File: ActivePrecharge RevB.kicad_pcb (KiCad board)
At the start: 2 copper layers, 59 parts, among them IC1 AMC1350DWVR, IC2 AMC1350DWVR, U1 LT1963AEST-3.3_TRPBF, U2 TLV9001IDBVR, U3 TLV9001IDBVR

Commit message: First Initial PCB Layout Finished
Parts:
- removed D5, D6: LED, LED_SMD:LED_0603_1608Metric_Pad1.05x0.95mm_HandSolder
- removed HV_Connector1: Conn_01x03, Connector_Molex:Molex_Nano-Fit_105309-xx03_1x03_P2.50mm_Vertical
- removed Motor_Contactor_Connector1, Precharge_Contactor_Connector1: Conn_01x04, Connector_Molex:Molex_Nano-Fit_105309-xx04_1x04_P2.50mm_Vertical
- removed R12, R14: 10k, Resistor_SMD:R_0603_1608Metric_Pad0.98x0.95mm_HandSolder
- removed R13: 15k, Resistor_SMD:R_0603_1608Metric_Pad0.98x0.95mm_HandSolder
- removed R15, R16: 10, Resistor_SMD:R_0603_1608Metric_Pad0.98x0.95mm_HandSolder
- removed VCU_Connector1: Conn_02x06_Counter_Clockwise, Connector_Molex:Molex_Nano-Fit_105310-xx12_2x06_P2.50mm_Vertical
- added C17: 100nF, Capacitor_SMD:C_0603_1608Metric_Pad1.08x0.95mm_HandSolder, F.Cu at (162.7, 100.3)
- added C20: 0.1uF, Capacitor_SMD:C_0603_1608Metric_Pad1.08x0.95mm_HandSolder, F.Cu at (157.5, 108.9)
- added C21: 0.47uF, Capacitor_SMD:C_0603_1608Metric_Pad1.08x0.95mm_HandSolder, F.Cu at (159.1, 111.4)
- added C22: 10nF, Capacitor_SMD:C_0603_1608Metric_Pad1.08x0.95mm_HandSolder, F.Cu at (180.2, 95.1)
- added C23: 10nF, Capacitor_SMD:C_0603_1608Metric_Pad1.08x0.95mm_HandSolder, F.Cu at (179.7, 105.4)
- added F3: 15A, ActivePrecharge-RevB:FUSE_3568, F.Cu at (170.2, 80.5)
- added H1: MountingHole_Pad, MountingHole:MountingHole_3.2mm_M3_Pad_TopBottom, F.Cu at (104.0, 63.6)
- added H2: MountingHole_Pad, MountingHole:MountingHole_3.2mm_M3_Pad_TopBottom, F.Cu at (192.8, 63.6)
- added H3: MountingHole_Pad, MountingHole:MountingHole_3.2mm_M3_Pad_TopBottom, F.Cu at (103.7, 116.3)
- added H4: MountingHole_Pad, MountingHole:MountingHole_3.2mm_M3_Pad_TopBottom, F.Cu at (193.0, 116.3)
- added IC3: ZXRE160AET5TA, ActivePrecharge-RevB:SOT95P280X100-5N, F.Cu at (161.6, 108.7)
- added J1: HVConnector, Connector_Molex:Molex_Nano-Fit_105309-xx03_1x03_P2.50mm_Vertical, F.Cu at (109.9, 71.8)
- added J2: ExportConnector, Connector_Molex:Molex_Nano-Fit_105310-xx12_2x06_P2.50mm_Vertical, F.Cu at (187.8, 84.2)
- added J3: PrechargeContactor, Connector_Molex:Molex_Nano-Fit_105309-xx04_1x04_P2.50mm_Vertical, F.Cu at (183.2, 70.0)
- added J4: MainContactor, Connector_Molex:Molex_Nano-Fit_105309-xx04_1x04_P2.50mm_Vertical, F.Cu at (190.8, 108.7)
- added R18: 1k, Resistor_SMD:R_0603_1608Metric_Pad0.98x0.95mm_HandSolder, F.Cu at (161.6, 106.1)
- added R19: 5.1k, Resistor_SMD:R_0603_1608Metric_Pad0.98x0.95mm_HandSolder, F.Cu at (162.9, 113.1)
- added R20: 15k, Resistor_SMD:R_0603_1608Metric_Pad0.98x0.95mm_HandSolder, F.Cu at (159.1, 113.1)
- added R21: 2.49k, Resistor_SMD:R_0603_1608Metric_Pad0.98x0.95mm_HandSolder, F.Cu at (170.9, 94.0)
- added R22: 15k, Resistor_SMD:R_0603_1608Metric_Pad0.98x0.95mm_HandSolder, F.Cu at (170.9, 95.9)
- added R23: 2.49k, Resistor_SMD:R_0603_1608Metric_Pad0.98x0.95mm_HandSolder, F.Cu at (175.5, 86.6)
- added R24: 15k, Resistor_SMD:R_0603_1608Metric_Pad0.98x0.95mm_HandSolder, F.Cu at (175.5, 90.8)
- added R25: 10, Resistor_SMD:R_0603_1608Metric_Pad0.98x0.95mm_HandSolder, F.Cu at (180.2, 93.1)
- added R26: 2.49k, Resistor_SMD:R_0603_1608Metric_Pad0.98x0.95mm_HandSolder, F.Cu at (170.9, 106.1)
- added R27: 2.49k, Resistor_SMD:R_0603_1608Metric_Pad0.98x0.95mm_HandSolder, F.Cu at (170.9, 99.0)
- added R28: 15k, Resistor_SMD:R_0603_1608Metric_Pad0.98x0.95mm_HandSolder, F.Cu at (170.9, 102.0)
- added R29: 15k, Resistor_SMD:R_0603_1608Metric_Pad0.98x0.95mm_HandSolder, F.Cu at (170.9, 107.7)
- added R30: 10, Resistor_SMD:R_0603_1608Metric_Pad0.98x0.95mm_HandSolder, F.Cu at (179.7, 103.5)
- added TP10: 3V3, TestPoint:TestPoint_Pad_1.0x1.0mm, F.Cu at (168.4, 70.8)
- added TP11: LVGND, TestPoint:TestPoint_Pad_1.0x1.0mm, F.Cu at (173.9, 112.2)
- C1, C2: footprint ActivePrecharge-RevB:CAPC1709X100N -> Capacitor_SMD:C_0805_2012Metric_Pad1.18x1.45mm_HandSolder
- C10, C11: value 1uF -> 1nF
- C13, C14, C6: value 100nF -> 1uF
- C15: value 10nF -> 1uF
- C16: value 10nF -> 100nF
- C3, C4: footprint Capacitor_SMD:C_0603_1608Metric_Pad1.08x0.95mm_HandSolder -> ActivePrecharge-RevB:CAPC1709X100N
- C5: value 100nF -> 1uF; footprint Capacitor_SMD:C_0603_1608Metric_Pad1.08x0.95mm_HandSolder -> ActivePrecharge-RevB:CAPC1709X100N
- C7: value 1nF -> 1uF
- C8: value 1nF -> 100nF
- C9: value 1uF -> 100nF
- D2, D3: value RSX068MP2STR -> LED; footprint ActivePrecharge-RevB:RSX068MP2STR -> LED_SMD:LED_0603_1608Metric_Pad1.05x0.95mm_HandSolder
- F1, F2: value Fuse -> 15A
- R10, R8: value 2.49k -> 100k
- R11: value 15k -> 2.49k
- R4: value 120 -> 330; footprint Resistor_SMD:R_0603_1608Metric_Pad0.98x0.95mm_HandSolder -> ActivePrecharge-RevB:RES_PWR263S-35-3300F
- R5: value 768 -> 1k
- R6: value 120 -> 1k
- R7: value 100k -> 1k
- R9: value 100k -> 2.49k
- U1: value LT1963AEST-3.3_TRPBF -> LT1963AEST-3.3#TRPBF
- moved TP1 72.9 mm to (116.0, 112.2)
- moved TP2 71.4 mm to (110.0, 112.2)
- moved TP7 69.8 mm to (147.8, 113.0), turned to 180 degrees
- moved R4 69.3 mm to (127.3, 109.6)
- moved TP3 63.5 mm to (116.0, 108.8)
- moved TP9 63.2 mm to (170.2, 112.2)
- moved R11 63.0 mm to (138.4, 101.6), turned to 90 degrees
- moved C15 61.6 mm to (165.7, 100.3), turned to -90 degrees
- moved C9 57.3 mm to (141.5, 97.8), turned to 90 degrees
- moved C11 55.8 mm to (146.0, 101.5), turned to -90 degrees
- moved C7 50.8 mm to (141.5, 101.5), turned to -90 degrees
- moved C16 50.6 mm to (166.7, 91.0), turned to -90 degrees
- moved C10 49.2 mm to (146.0, 92.4), turned to -90 degrees
- moved U3 47.1 mm to (175.3, 104.5)
- moved C13 47.0 mm to (146.0, 97.7), turned to 90 degrees
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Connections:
- C10 pad 1: REG_3V3 -> /Voltage_Sense/Vin1
- C11 pad 1: 3V3 -> /Voltage_Sense/Vin2
- C11 pad 2: LVGND -> HVGND
- C12 pad 1: 3V3 -> REG_3V3
- C12 pad 2: LVGND -> HVGND
- C13 pad 1: 3V3 -> REG_3V3
- C13 pad 2: LVGND -> HVGND
- C15 pad 1: /VOut1 -> 3V3
- C16 pad 1: /VOut2 -> 3V3
- C3 pad 1: /Voltage_Sense/Vin1 -> 3V3
- C3 pad 2: HVGND -> LVGND
- C4 pad 1: /Voltage_Sense/Vin2 -> HVGND
- C4 pad 2: HVGND -> ISO_5V
- C5 pad 1: REG_3V3 -> 3V3
- C5 pad 2: HVGND -> LVGND
- C6 pad 1: REG_3V3 -> /Voltage_Sense/Vin1
- C7 pad 1: /Voltage_Sense/Vin1 -> /Voltage_Sense/Vin2
- C8 pad 1: /Voltage_Sense/Vin2 -> REG_3V3
- D2 pad 1: Net-(D2-K) -> HVGND
- D2 pad 2: HVGND -> Net-(D2-A)
- D3 pad 1: HV- -> HVGND
- F2 pad 2: Net-(D3-A) -> HV-
- R10 pad 1: HVGND -> /Voltage_Sense/Vin2
- R10 pad 2: /Voltage_Sense/Vin2 -> HV-
- R11 pad 1: Net-(U2-OUT) -> HVGND
- R11 pad 2: Net-(U2-IN-) -> /Voltage_Sense/Vin2
- R4 pad 1: REG_3V3 -> HV-
- R4 pad 2: Net-(D4-A) -> HV+
- R5 pad 1: ISO_5V -> REG_3V3
- R5 pad 2: Net-(D5-A) -> Net-(D2-A)
- R6 pad 1: 3V3 -> ISO_5V
- R6 pad 2: Net-(D6-A) -> Net-(D3-A)
- R7 pad 1: /Voltage_Sense/Vin1 -> 3V3
- R7 pad 2: HV+ -> Net-(D4-A)
- R8 pad 1: HVGND -> /Voltage_Sense/Vin1
- R8 pad 2: /Voltage_Sense/Vin1 -> HV+
- R9 pad 1: /Voltage_Sense/Vin2 -> HVGND
- R9 pad 2: HV- -> /Voltage_Sense/Vin1
- U1 pad 4: HVGND -> (no net)
- U2 pad 1: Net-(U2-OUT) -> Net-(U2-+)
- U2 pad 2: LVGND -> Net-(U2--)
- U2 pad 3: /Voltage_Sense/V1 -> 3V3
- U2 pad 4: Net-(U2-IN-) -> LVGND
- U2 pad 5: 3V3 -> Net-(R22-Pad1)
- U3 pad 2: LVGND -> Net-(U3--)
- U3 pad 3: /Voltage_Sense/V2 -> 3V3
- U3 pad 4: Net-(U3-IN-) -> LVGND
- U3 pad 5: 3V3 -> Net-(R29-Pad1)
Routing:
- net 3V3: track 0.00 -> 77.1 mm, vias 0 -> 4
- net HV+: track 0.00 -> 38.9 mm, vias 0 -> 2
- net /Voltage_Sense/Vin1: track 0.00 -> 37.6 mm
- net REG_3V3: track 0.00 -> 36.6 mm, vias 0 -> 3
- net /Voltage_Sense/V1: track 0.00 -> 36.3 mm
- net REG_0V8: track 0.00 -> 32.6 mm, vias 0 -> 2
- net /Pre-: track 0.00 -> 31.1 mm
- net HV-: track 0.00 -> 28.1 mm, vias 0 -> 3
- net /VOut2: track 0.00 -> 27.5 mm
- net /Voltage_Sense/Vin2: track 0.00 -> 25.6 mm
- net /Motor-: track 0.00 -> 25.5 mm
- net /MotorSense-: track 0.00 -> 25.0 mm
- net /PreSense-: track 0.00 -> 23.5 mm
- net /Voltage_Sense/V2: track 0.00 -> 22.9 mm, vias 0 -> 2
- net /PreSense+: track 0.00 -> 22.0 mm
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- added copper zone on B.Cu, net 3V3
- added copper zone on F.Cu, net HV+
- added copper zone on F.Cu, net HV-
- added copper zone on F.Cu, net HVGND
- added copper zone on F.Cu, net LVGND
- added copper zone on B.Cu, net REG_3V3
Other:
- board outline added: 98 x 61 mm

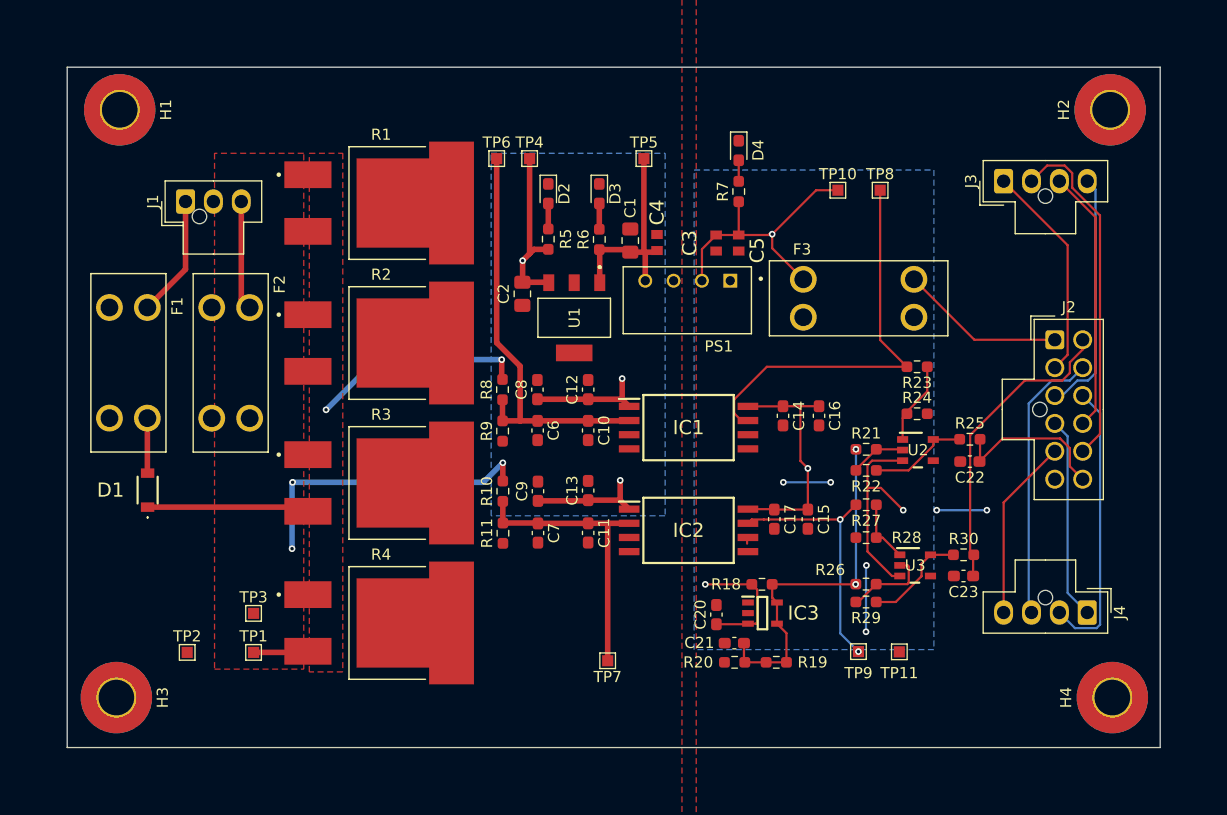
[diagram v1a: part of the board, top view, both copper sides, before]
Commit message: All layout changes made except new symbol for precharge resistors for heat dissipation and new fuses
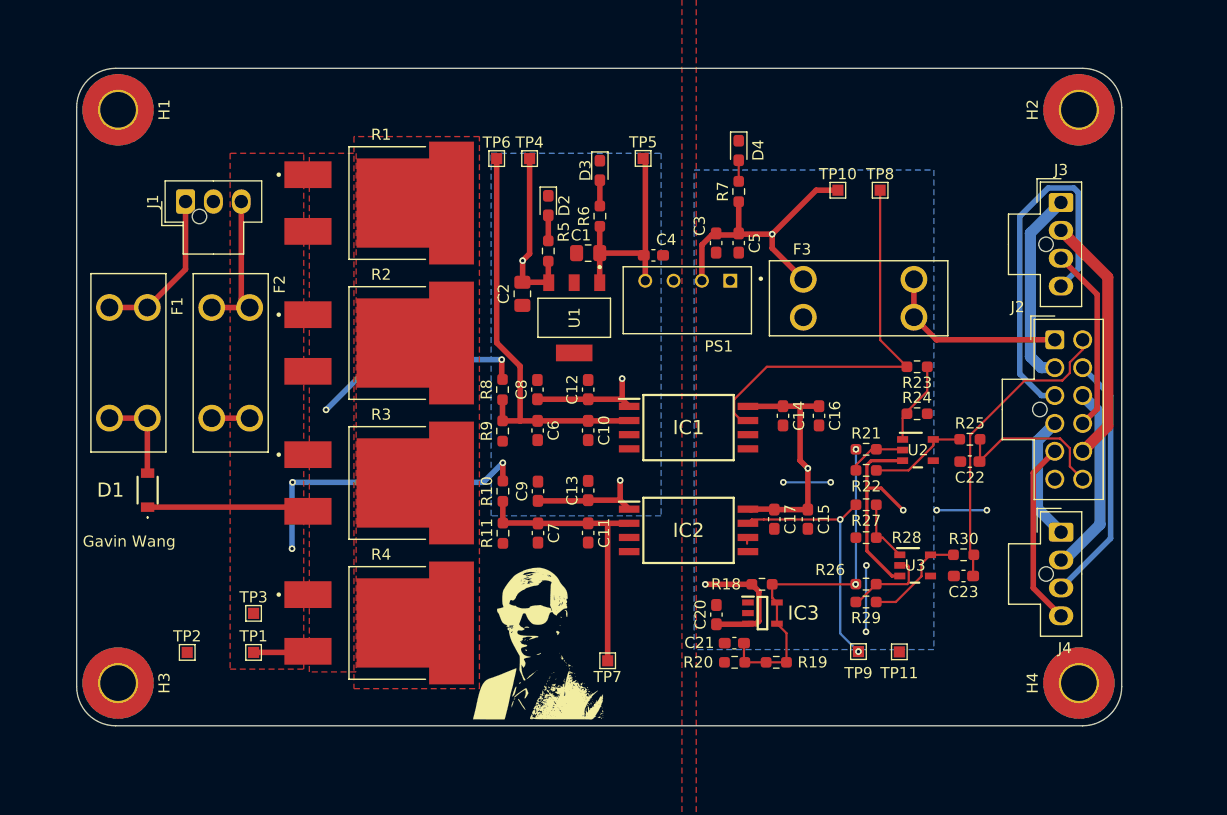
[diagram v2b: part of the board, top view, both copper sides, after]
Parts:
- added LOGO1: Dr. Hallock, UTSVT-Logos:Hallock_Image_Tiny, F.Cu at (141.0, 111.3)
- added LOGO2: Dr. Hallock, UTSVT-Logos:LHRs_LOGO, F.Cu at (117.5, 63.2)
- C3, C4, C5: footprint ActivePrecharge-RevB:CAPC1709X100N -> Capacitor_SMD:C_0603_1608Metric_Pad1.08x0.95mm_HandSolder
- F1, F2, F3: value 15A -> 1.5A
- moved J4 7.58 mm to (188.4, 101.5), turned to 0 degrees
- moved J3 5.49 mm to (188.4, 71.9), turned to 0 degrees
- moved C1 3.94 mm to (146.0, 76.5), turned to 180 degrees
- moved H4 3.27 mm to (190.0, 115.0)
- moved H2 2.80 mm to (190.0, 63.6)
- moved D3 2.09 mm to (147.1, 69.0)
- moved R6 2.09 mm to (147.1, 73.1)
- moved H3 1.31 mm to (103.8, 115.0)
- moved C4 1.20 mm to (151.8, 76.7), turned to 180 degrees
- moved D2 1.06 mm to (142.4, 72.2)
- moved R5 1.06 mm to (142.4, 76.3)
- moved H1 0.15 mm to (103.8, 63.6)
- moved TP5 0.07 mm to (150.9, 68.0)
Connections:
- U1 pad 4: (no net) -> HVGND
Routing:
- net /PreSense+: track 22.0 -> 33.6 mm
- net /Pre-: track 31.1 -> 22.5 mm
- net /Motor-: track 25.5 -> 17.0 mm
- net /Motor+: track 18.2 -> 11.3 mm
- net /PreSense-: track 23.5 -> 16.7 mm
- net Net-(D1-A): track 4.94 -> 8.34 mm
- net Net-(J1-Pin_3): track 9.82 -> 13.2 mm
- net Net-(J1-Pin_1): track 10.9 -> 14.3 mm
- net HV-: track 28.1 -> 31.5 mm
- net /MotorSense-: track 25.0 -> 22.6 mm
- net /Pre+: track 19.6 -> 17.6 mm
- net Net-(J2-Pin_1): track 14.9 -> 16.9 mm
- net 3V3: track 77.1 -> 78.7 mm
- net ISO_5V: track 19.3 -> 20.3 mm
- added copper zone on F.Cu, net (none)
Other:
- board size 98 x 61 mm -> 93.7 x 58.9 mm
- board text added: "Gavin Wang"

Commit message: All new comments addressed
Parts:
- moved V1 3.81 mm to (172.2, 67.0)
- moved 3V3 3.81 mm to (168.4, 67.0)
- moved LOGO2 2.64 mm to (115.3, 64.8)
- moved REG_3V3 2.50 mm to (143.1, 67.0)
- moved ExportConnector 1.16 mm to (187.8, 83.1)
- moved PrechargeContactor 1.16 mm to (188.3, 70.8)
- moved MainContactor 1.16 mm to (188.4, 100.3)
- moved Vin1 0.97 mm to (137.8, 67.0)
- moved ISO_5V 0.96 mm to (151.0, 67.0)
- moved C22 0.53 mm to (179.7, 95.1)
- moved R25 0.53 mm to (179.7, 93.1)
- moved Vin2 0.50 mm to (147.8, 112.5)
- moved V2 0.42 mm to (170.5, 112.5)
- moved LVGND 0.30 mm to (173.9, 112.5)
- renumbered TP10 to 3V3, J2 to ExportConnector, TP1 to HV+, TP3 to HV-, J1 to HVConnector, TP2 to HV_GND, TP5 to ISO_5V, TP11 to LVGND, J4 to MainContactor, J3 to PrechargeContactor, TP4 to REG_3V3, TP8 to V1, TP9 to V2, TP6 to Vin1, TP7 to Vin2
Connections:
- R1 pad 3: (no net) -> /HEAT_DISSIPATION
- R2 pad 3: (no net) -> /HEAT_DISSIPATION
- R3 pad 3: (no net) -> /HEAT_DISSIPATION
- R4 pad 3: (no net) -> /HEAT_DISSIPATION
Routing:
- net LVGND: track 15.3 -> 4.84 mm
- net HV-: track 31.5 -> 25.6 mm, vias 3 -> 7
- net REG_3V3: track 36.6 -> 32.4 mm, vias 3 -> 5
- net /Voltage_Sense/V1: track 36.3 -> 40.1 mm
- net 3V3: track 78.7 -> 75.5 mm, vias 4 -> 3
- net /VOut2: track 27.5 -> 29.1 mm
- net /Voltage_Sense/V2: track 22.9 -> 24.2 mm
- net /Voltage_Sense/Vin1: track 37.6 -> 38.6 mm
- net ISO_5V: track 20.3 -> 21.2 mm
- net REG_0V8: track 32.6 -> 33.4 mm
- net Net-(J2-Pin_1): track 16.9 -> 16.3 mm
- net Net-(R22-Pad1): track 8.95 -> 8.43 mm
- net /Voltage_Sense/Vin2: track 25.6 -> 25.1 mm
- net HVGND: vias 0 -> 1
- net /HEAT_DISSIPATION: vias 0 -> 24
- added copper zone on B.Cu, net /HEAT_DISSIPATION
- added copper zone on F.Cu, net /HEAT_DISSIPATION
- added copper zone on B.Cu, net HV-
- added copper zone on B.Cu, net HVGND
- added copper zone on B.Cu, net LVGND
- added copper zone on F.Cu, net REG_3V3
- removed copper zone on F.Cu, net (none)
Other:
- board text added: "1.5A"

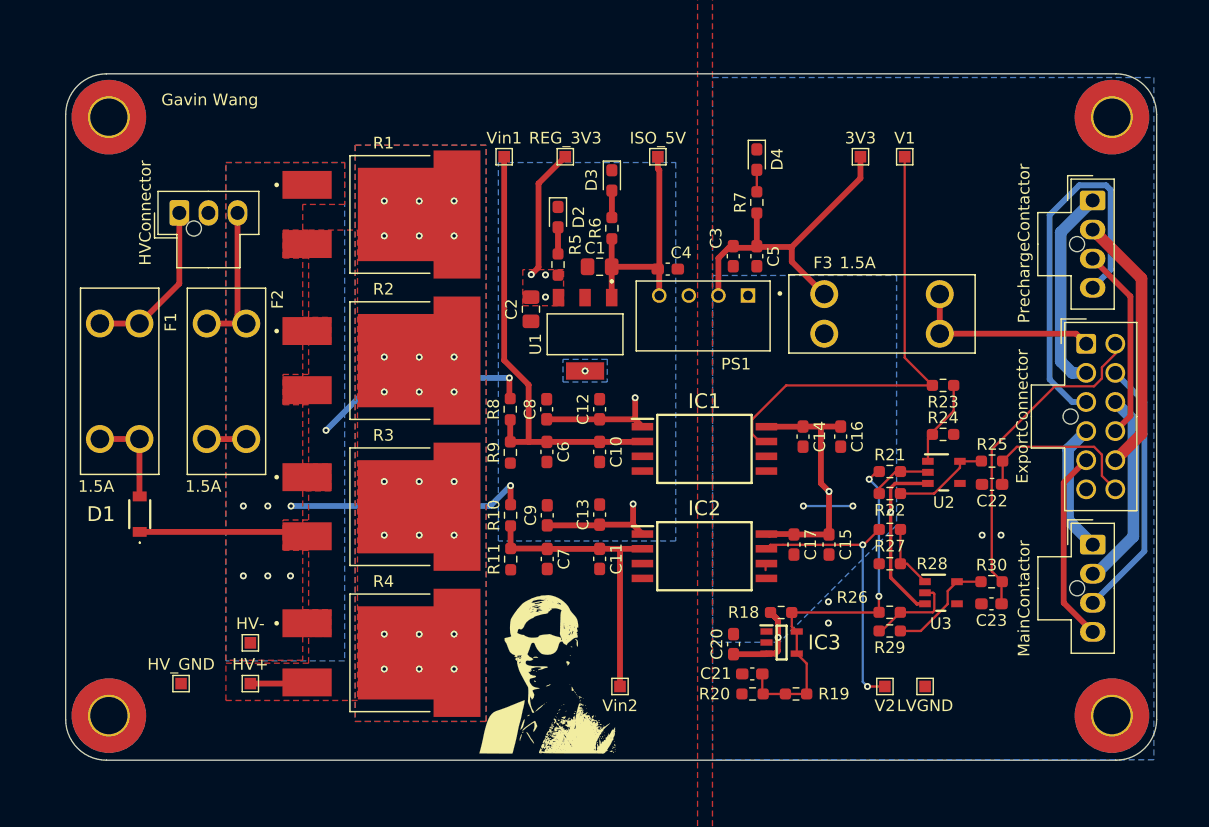
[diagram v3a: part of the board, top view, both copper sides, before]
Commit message: LVGND Stitching vias added to edges
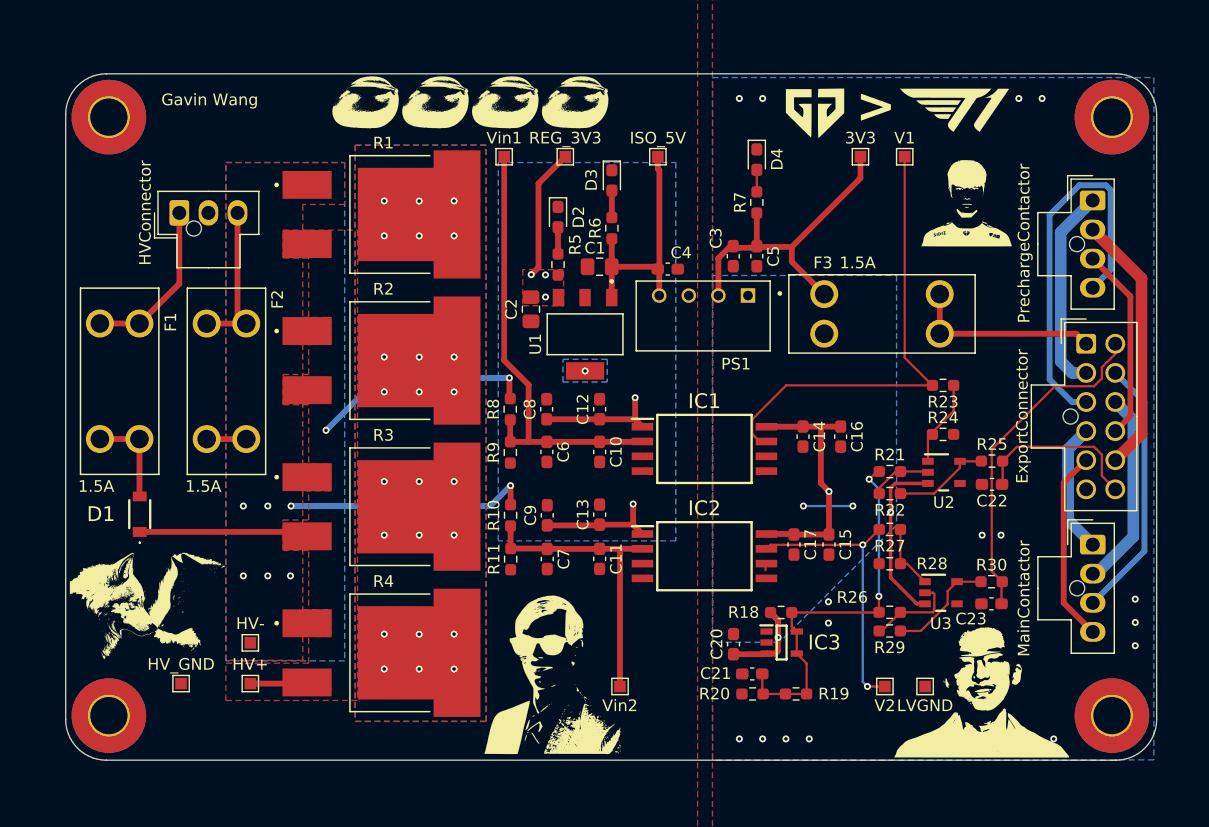
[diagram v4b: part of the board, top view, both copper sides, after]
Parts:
- added G***: LOGO, LOGO, F.Cu at (164.5, 63.0)
- added G***: LOGO, LOGO, F.Cu at (177.2, 71.0)
- added G***: LOGO, LOGO, F.Cu at (176.5, 63.0)
- added G***: LOGO, LOGO, F.Cu at (178.8, 112.0)
- added G***: LOGO, LOGO, F.Cu at (144.0, 62.6)
- added G***: LOGO, LOGO, F.Cu at (138.0, 62.6)
- added G***: LOGO, LOGO, F.Cu at (126.0, 62.6)
- added G***: LOGO, LOGO, F.Cu at (108.0, 105.7)
- added G***: LOGO, LOGO, F.Cu at (132.0, 62.6)
- moved LOGO1 0.44 mm to (141.5, 111.3)
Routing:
- net LVGND: vias 6 -> 18
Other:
- board text added: ">"

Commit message: Implemented all changes
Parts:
- added MCont: LED, LED_SMD:LED_0603_1608Metric_Pad1.05x0.95mm_HandSolder, F.Cu at (181.1, 102.2)
- added PreCont: LED, LED_SMD:LED_0603_1608Metric_Pad1.05x0.95mm_HandSolder, F.Cu at (182.8, 68.9)
- added R12: 1k, Resistor_SMD:R_0603_1608Metric_Pad0.98x0.95mm_HandSolder, F.Cu at (182.8, 67.3)
- added R13: 1k, Resistor_SMD:R_0603_1608Metric_Pad0.98x0.95mm_HandSolder, F.Cu at (181.1, 100.6)
- C20: value 0.1uF -> 100nF
- TP1: renamed from HV+; footprint TestPoint:TestPoint_Pad_1.0x1.0mm -> TestPoint:TestPoint_THTPad_D1.0mm_Drill0.5mm
- TP10: renamed from 3V3; footprint TestPoint:TestPoint_Pad_1.0x1.0mm -> TestPoint:TestPoint_THTPad_D1.0mm_Drill0.5mm
- TP11: renamed from LVGND; footprint TestPoint:TestPoint_Pad_1.0x1.0mm -> TestPoint:TestPoint_THTPad_D1.0mm_Drill0.5mm
- TP2: renamed from HV_GND; footprint TestPoint:TestPoint_Pad_1.0x1.0mm -> TestPoint:TestPoint_THTPad_D1.0mm_Drill0.5mm
- TP3: renamed from HV-; footprint TestPoint:TestPoint_Pad_1.0x1.0mm -> TestPoint:TestPoint_THTPad_D1.0mm_Drill0.5mm
- TP4: renamed from REG_3V3; footprint TestPoint:TestPoint_Pad_1.0x1.0mm -> TestPoint:TestPoint_THTPad_D1.0mm_Drill0.5mm
- TP5: renamed from ISO_5V; footprint TestPoint:TestPoint_Pad_1.0x1.0mm -> TestPoint:TestPoint_THTPad_D1.0mm_Drill0.5mm
- TP6: renamed from Vin1; footprint TestPoint:TestPoint_Pad_1.0x1.0mm -> TestPoint:TestPoint_THTPad_D1.0mm_Drill0.5mm
- TP7: renamed from Vin2; footprint TestPoint:TestPoint_Pad_1.0x1.0mm -> TestPoint:TestPoint_THTPad_D1.0mm_Drill0.5mm
- TP8: renamed from V1; footprint TestPoint:TestPoint_Pad_1.0x1.0mm -> TestPoint:TestPoint_THTPad_D1.0mm_Drill0.5mm
- TP9: renamed from V2; footprint TestPoint:TestPoint_Pad_1.0x1.0mm -> TestPoint:TestPoint_THTPad_D1.0mm_Drill0.5mm
- moved H2 4.66 mm to (194.7, 63.6)
- moved H4 4.66 mm to (194.7, 115.0)
- moved C8 4.65 mm to (146.1, 88.9)
- moved C9 4.61 mm to (146.1, 98.1)
- moved C16 2.90 mm to (163.8, 91.0)
- moved C5 2.42 mm to (157.1, 75.2), turned to 0 degrees
- moved G*** 2.40 mm to (181.2, 111.9)
- moved R21 2.35 mm to (168.6, 94.0)
- moved R22 2.35 mm to (168.6, 95.9)
- moved R27 2.35 mm to (168.6, 99.0)
- moved C22 2.35 mm to (177.3, 95.1)
- moved C23 2.35 mm to (177.3, 105.4)
- moved R23 2.35 mm to (173.1, 86.6)
- moved R24 2.35 mm to (173.1, 90.8)
- moved R25 2.35 mm to (177.3, 93.1)
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- renumbered D4 to 3V3, D3 to ISO_5V, HVConnector to J1, ExportConnector to J2, PrechargeContactor to J3, MainContactor to J4, D2 to REG_3V3
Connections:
- J2 pad 10: /PreSense- -> /MotorSense-
- J2 pad 11: /Pre- -> /Motor-
- J2 pad 12: /VOut1 -> /VOut2
- J2 pad 2: /Pre+ -> /PreSense+
- J2 pad 3: /PreSense+ -> /Pre+
- J2 pad 4: /Motor+ -> /MotorSense+
- J2 pad 5: /MotorSense+ -> /Motor+
- J2 pad 7: /VOut2 -> /VOut1
- J2 pad 8: /MotorSense- -> /PreSense-
- J2 pad 9: /Motor- -> /Pre-
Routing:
- net /PreSense+: track 33.6 -> 8.62 mm
- net 3V3: track 75.5 -> 64.9 mm
- net /VOut2: track 29.1 -> 18.6 mm
- net REG_3V3: track 32.4 -> 24.1 mm
- net /Pre+: track 17.6 -> 25.4 mm
- net /MotorSense-: track 22.6 -> 17.6 mm
- net /PreSense-: track 16.7 -> 11.7 mm
- net LVGND: track 4.84 -> 0.59 mm, vias 18 -> 17
- net /Motor+: track 11.3 -> 15.2 mm
- net /VOut1: track 14.7 -> 18.1 mm
- net /Voltage_Sense/V1: track 40.1 -> 36.7 mm
- net /MotorSense+: track 16.6 -> 19.6 mm
- net REG_0V8: track 33.4 -> 31.1 mm
- net /Motor-: track 17.0 -> 18.7 mm
- net Net-(D5-A): track 0.00 -> 1.56 mm
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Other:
- board size 93.7 x 58.9 mm -> 98.4 x 58.9 mm
- board text added: "3V3"
- board text added: "Batt"
- board text added: "Gavin Wang October 2025"
- board text added: "HVGND"
- board text added: "LVGND"
- board text added: "MSense+"
- board text added: "MSense-"
- board text added: "Motor"
- board text added: "Motor+"
- board text added: "Motor-"
- board text added: "PSense+"
- board text added: "PSense-"
- board text added: "Pre+"
- board text added: "Pre-"
- board text added: "VOut1"
- board text added: "VOut2"
- board text removed: "Gavin Wang"
